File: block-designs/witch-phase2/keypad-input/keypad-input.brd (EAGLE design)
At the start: 160 x 100 mm, 33 parts, among them SW0 SWITCH-MOMENTARY-212MM, SW1 SWITCH-MOMENTARY-212MM, SW2 SWITCH-MOMENTARY-212MM, SW3 SWITCH-MOMENTARY-212MM, SW4 SWITCH-MOMENTARY-212MM, SW5 SWITCH-MOMENTARY-212MM, SW6 SWITCH-MOMENTARY-212MM, SW7 SWITCH-MOMENTARY-212MM, SW8 SWITCH-MOMENTARY-212MM, SW9 SWITCH-MOMENTARY-212MM

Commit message: change polarity of buttons to active high
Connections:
- net GND: now also R1.2, R10.2, R11.2, R12.2, R13.2, R14.2, R15.2, R16.2, R2.2, R3.2, R4.2, R5.2, R6.2, R7.2, R8.2, R9.2; no longer SW-EXEC.1, SW-MINUS.1, SW-ORDER.1, SW-PLUS.1, SW-RESET.1, SW-SPACE.1, SW0.1, SW1.1, SW2.1, SW3.1, SW4.1, SW5.1, SW6.1, SW7.1, SW8.1, SW9.1
- net VCC: now also SW-EXEC.1, SW-MINUS.1, SW-ORDER.1, SW-PLUS.1, SW-RESET.1, SW-SPACE.1, SW0.1, SW1.1, SW2.1, SW3.1, SW4.1, SW5.1, SW6.1, SW7.1, SW8.1, SW9.1; no longer R1.2, R10.2, R11.2, R12.2, R13.2, R14.2, R15.2, R16.2, R2.2, R3.2, R4.2, R5.2, R6.2, R7.2, R8.2, R9.2
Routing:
- added copper zone on layer 1, net GND
- added copper zone on layer 16, net VCC
- removed copper zone on layer 16, net GND
- removed copper zone on layer 1, net VCC
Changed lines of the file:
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@@
 <signals>
 <signal name="VCC">
-<contactref element="R1" pad="2"/>
-<contactref element="R2" pad="2"/>
-<contactref element="R3" pad="2"/>
-<contactref element="R4" pad="2"/>
-<contactref element="R5" pad="2"/>
-<contactref element="R6" pad="2"/>
-<contactref element="R7" pad="2"/>
-<contactref element="R8" pad="2"/>
-<contactref element="R9" pad="2"/>
-<contactref element="R10" pad="2"/>
-<contactref element="R11" pad="2"/>
-<contactref element="R12" pad="2"/>
-<contactref element="R13" pad="2"/>
-<contactref element="R14" pad="2"/>
-<contactref element="R15" pad="2"/>
-<contactref element="R16" pad="2"/>
 <contactref element="JP1" pad="1"/>
-<polygon width="0.254" layer="1">
+<contactref element="SW1" pad="1"/>
+<contactref element="SW2" pad="1"/>
+<contactref element="SW3" pad="1"/>
+<contactref element="SW4" pad="1"/>
+<contactref element="SW5" pad="1"/>
+<contactref element="SW6" pad="1"/>
+<contactref element="SW7" pad="1"/>
+<contactref element="SW8" pad="1"/>
+<contactref element="SW9" pad="1"/>
+<contactref element="SW0" pad="1"/>
+<contactref element="SW-ORDER" pad="1"/>
+<contactref element="SW-EXEC" pad="1"/>
+<contactref element="SW-SPACE" pad="1"/>
+<contactref element="SW-PLUS" pad="1"/>
+<contactref element="SW-MINUS" pad="1"/>
+<contactref element="SW-RESET" pad="1"/>
+<polygon width="0.254" layer="16">
 <vertex x="0" y="0"/>
 <vertex x="160.02" y="0"/>
@@
 </signal>
 <signal name="GND">
-<contactref element="SW1" pad="1"/>
-<contactref element="SW2" pad="1"/>
-<contactref element="SW3" pad="1"/>
-<contactref element="SW4" pad="1"/>
-<contactref element="SW5" pad="1"/>
-<contactref element="SW6" pad="1"/>
-<contactref element="SW7" pad="1"/>
-<contactref element="SW8" pad="1"/>
-<contactref element="SW9" pad="1"/>
-<contactref element="SW0" pad="1"/>
-<contactref element="SW-ORDER" pad="1"/>
-<contactref element="SW-EXEC" pad="1"/>
-<contactref element="SW-SPACE" pad="1"/>
-<contactref element="SW-PLUS" pad="1"/>
-<contactref element="SW-MINUS" pad="1"/>
-<contactref element="SW-RESET" pad="1"/>
 <contactref element="JP1" pad="18"/>
-<polygon width="0.254" layer="16">
+<contactref element="R1" pad="2"/>
+<contactref element="R2" pad="2"/>
+<contactref element="R9" pad="2"/>
+<contactref element="R10" pad="2"/>
+<contactref element="R3" pad="2"/>
+<contactref element="R11" pad="2"/>
+<contactref element="R4" pad="2"/>
+<contactref element="R12" pad="2"/>
+<contactref element="R5" pad="2"/>
+<contactref element="R13" pad="2"/>
+<contactref element="R6" pad="2"/>
+<contactref element="R14" pad="2"/>
+<contactref element="R7" pad="2"/>
+<contactref element="R15" pad="2"/>
+<contactref element="R8" pad="2"/>
+<contactref element="R16" pad="2"/>
+<polygon width="0.254" layer="1">
 <vertex x="0" y="0"/>
 <vertex x="160.02" y="0"/>

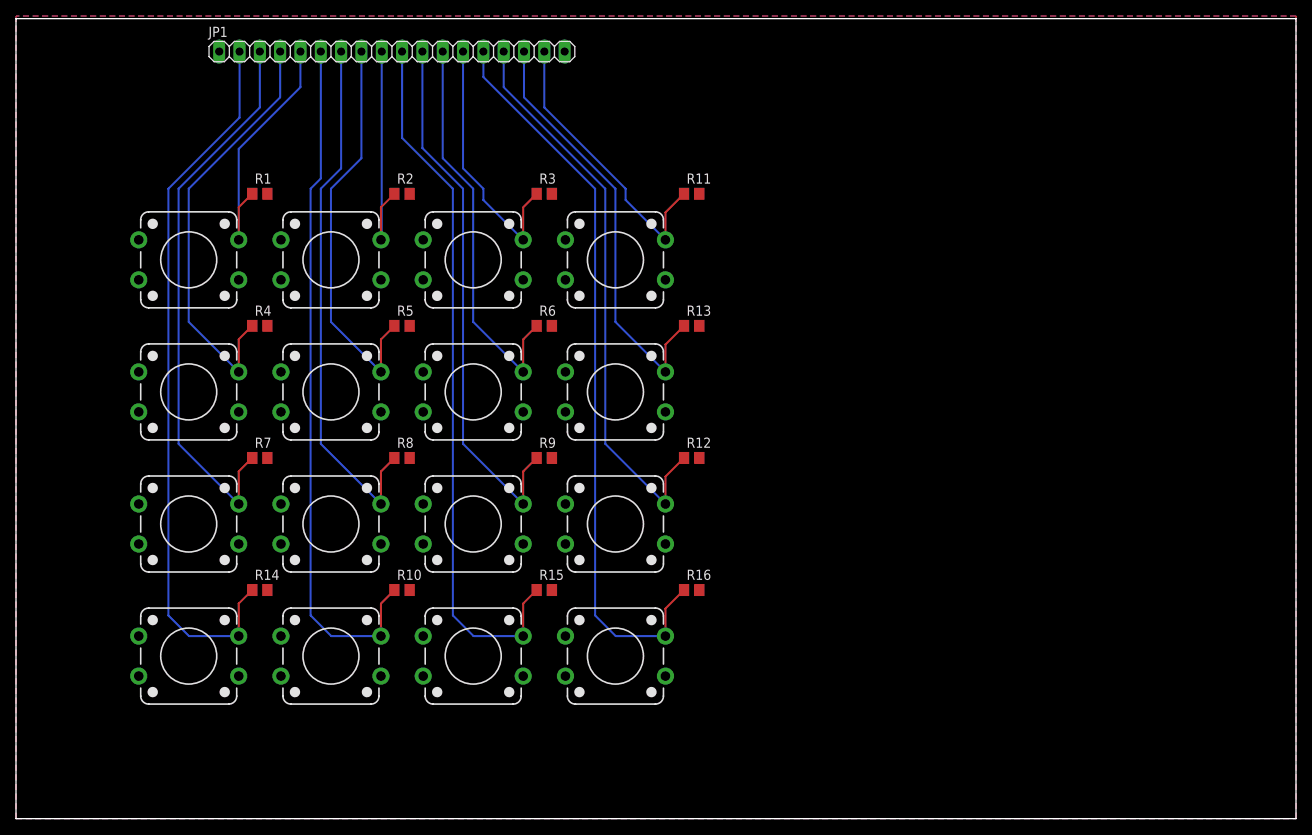
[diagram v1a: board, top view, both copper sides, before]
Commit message: reduce size of module and add mounting holes
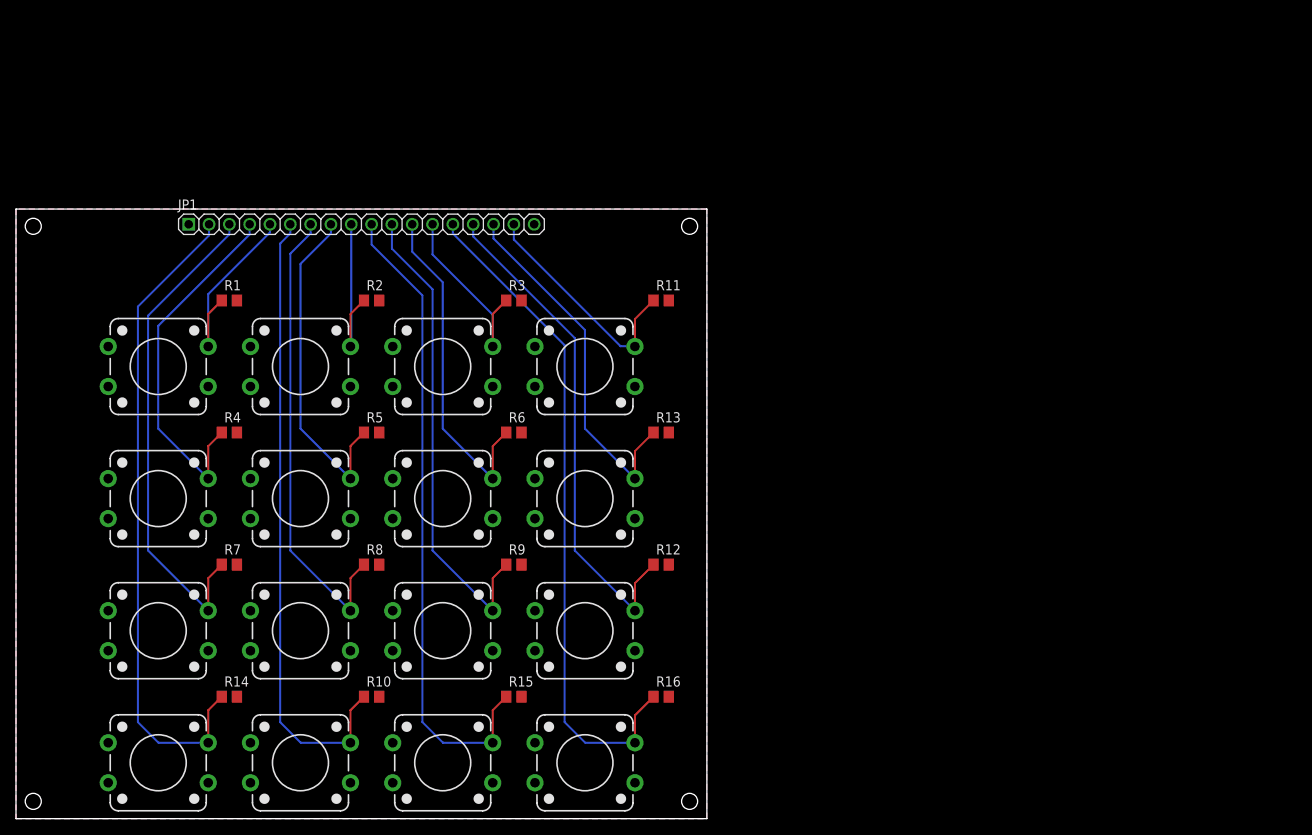
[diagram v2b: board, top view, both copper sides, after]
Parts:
- moved JP1 21.9 mm to (43.2, 74.3)
- moved R3 13.9 mm to (62.2, 64.8)
- moved R1 13.9 mm to (26.7, 64.8)
- moved R11 13.9 mm to (80.6, 64.8)
- moved R2 13.9 mm to (44.5, 64.8)
- moved R6 13.9 mm to (62.2, 48.3)
- moved R9 13.9 mm to (62.2, 31.8)
- moved R15 13.9 mm to (62.2, 15.2)
- moved R12 13.9 mm to (80.6, 31.8)
- moved R13 13.9 mm to (80.6, 48.3)
- moved R4 13.9 mm to (26.7, 48.3)
- moved R5 13.9 mm to (44.5, 48.3)
- moved R7 13.9 mm to (26.7, 31.8)
- moved R8 13.9 mm to (44.5, 31.8)
- moved SW-MINUS 13.9 mm to (53.3, 6.99)
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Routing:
- net SW2: track 30.0 -> 21.8 mm
- net SW1: track 33.2 -> 24.9 mm
- net SW9: track 68.2 -> 60.0 mm
- net SW3: track 33.1 -> 24.8 mm
- net SW8: track 67.2 -> 58.9 mm
- net SW7: track 70.3 -> 62.1 mm
- net SW5: track 50.7 -> 42.4 mm
- net SW4: track 53.8 -> 45.6 mm
- net SW-EXEC: track 71.6 -> 63.4 mm
- net SW6: track 50.7 -> 42.4 mm
- net SW-SPACE: track 54.1 -> 45.8 mm
- net SW0: track 87.3 -> 79.1 mm
- net SW-RESET: track 92.8 -> 84.6 mm
- net SW-PLUS: track 90.5 -> 82.2 mm
- net SW-MINUS: track 89.4 -> 81.2 mm
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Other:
- board size 160 x 100 mm -> 86.4 x 76.2 mm
- board text added: "Manual Entry Keypad"
